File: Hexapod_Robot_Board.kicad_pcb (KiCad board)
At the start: 4 copper layers, 100 x 80 mm, 88 parts, among them J1 USB-C, SW1 RESET, SW2 BOOT, U1 ESP32-S3, U2 BQ25886, U3 XL4015, U4 AMS1117-3.3, U5 PCA9685_1, U6 PCA9685_2

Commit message: fix: invert USB-C orientation, clear ESP32 antenna keepout, achieve 0 DRC/ERC violations, and update 3D/fab outputs
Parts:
- moved R_CC2 46.0 mm to (12.0, 6.50), turned to 0 degrees
- moved J1 30.0 mm to (20.0, 3.90), turned to 180 degrees
- moved R_CC1 30.0 mm to (12.0, 4.00), turned to 0 degrees
- moved LED_CHG 7.28 mm to (27.0, 4.00)
- moved LED_FULL 4.47 mm to (30.5, 4.00)
- moved R_CHG 4.18 mm to (27.0, 7.20)
- moved SW1 2.55 mm to (35.5, 5.50)
- moved SW2 2.50 mm to (64.5, 6.00)
- moved R_FULL 1.56 mm to (30.5, 7.20)
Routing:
- net GND: track 114.0 -> 79.7 mm, vias 42 -> 47
- net USB_D-: track 45.8 -> 66.2 mm, vias 3 -> 2
- net USB_D+: track 49.6 -> 65.4 mm
- net VBUS: track 81.3 -> 67.4 mm, vias 9 -> 4
- net CC1: track 14.8 -> 20.0 mm
- net CC2: track 14.1 -> 10.5 mm
- net ESP_EN: track 41.9 -> 38.4 mm
- net CHG_PG: track 23.6 -> 25.7 mm
- net ESP_IO0: track 44.8 -> 46.0 mm
- net CHG_STAT: track 19.0 -> 18.7 mm, vias 0 -> 2

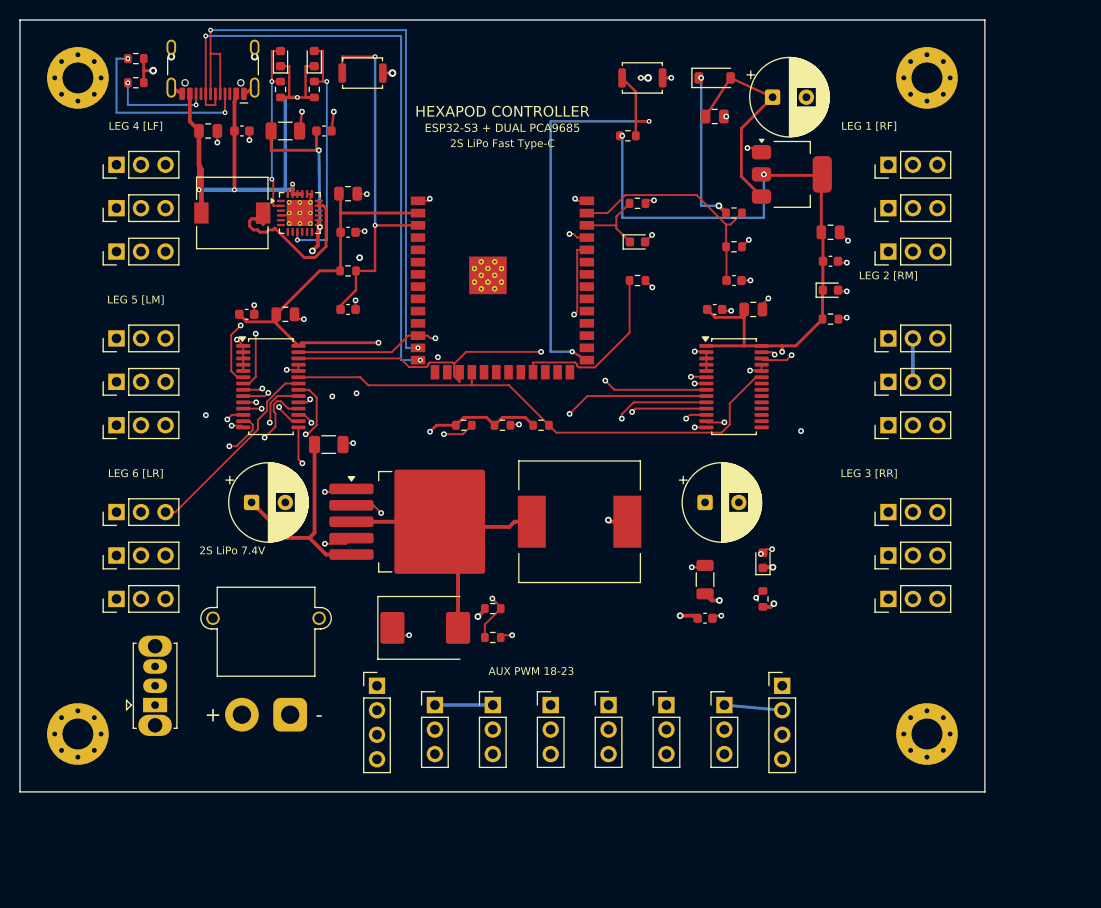
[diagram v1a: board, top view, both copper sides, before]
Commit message: feat(pcb): complete Rev 2.0 4-layer routing, achieve 0 DRC / 0 ERC, and export fabrication package
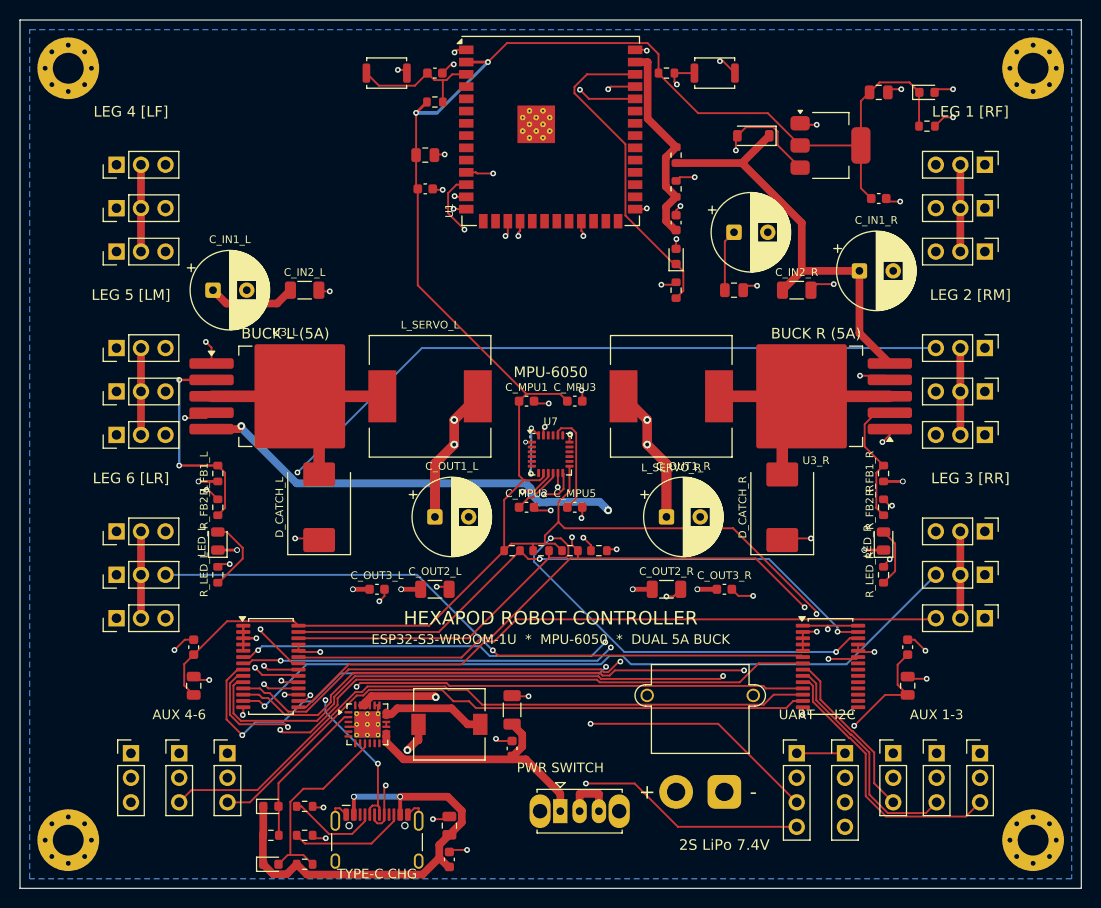
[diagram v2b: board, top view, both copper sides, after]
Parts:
- removed C_IN1: 100uF_25V, CP_Radial_D8.0mm_P3.50mm
- removed C_IN2: 22uF_25V, C_1206_3216Metric
- removed C_OUT1: 1000uF_10V, CP_Radial_D8.0mm_P3.50mm
- removed C_OUT2: 22uF_16V, C_1206_3216Metric
- removed C_OUT3: 100nF, Capacitor_SMD:C_0603_1608Metric
- removed D_CATCH: SS54, D_SMC
- removed LED_SERVO: Green, LED_0603_1608Metric
- removed L_SERVO: 10uH_10A, L_12x12mm_H8mm
- removed R_FB1: 10k_1%, R_0603_1608Metric
- removed R_FB2: 3.16k_1%, R_0603_1608Metric
- removed R_SERVO_LED: 1k, R_0603_1608Metric
- removed U3: XL4015, TO-263-5_TabPin3
- added C_IN1_L: 100uF_25V, Capacitor_THT:CP_Radial_D8.0mm_P3.50mm, F.Cu at (20.0, 28.0)
- added C_IN1_R: 100uF_25V, Capacitor_THT:CP_Radial_D8.0mm_P3.50mm, F.Cu at (87.0, 26.0)
- added C_IN2_L: 22uF_25V, Capacitor_SMD:C_1206_3216Metric, F.Cu at (29.5, 28.0)
- added C_IN2_R: 22uF_25V, Capacitor_SMD:C_1206_3216Metric, F.Cu at (80.5, 28.0)
- added C_MPU1: 100nF, Capacitor_SMD:C_0603_1608Metric, F.Cu at (52.5, 39.5)
- added C_MPU2: 100nF, Capacitor_SMD:C_0603_1608Metric, F.Cu at (52.5, 50.5)
- added C_MPU3: 100nF, Capacitor_SMD:C_0603_1608Metric, F.Cu at (57.5, 39.5)
- added C_MPU5: 2.2nF, Capacitor_SMD:C_0603_1608Metric, F.Cu at (57.5, 50.5)
- added C_OUT1_L: 1000uF_10V, Capacitor_THT:CP_Radial_D8.0mm_P3.50mm, F.Cu at (43.0, 51.5)
- added C_OUT1_R: 1000uF_10V, Capacitor_THT:CP_Radial_D8.0mm_P3.50mm, F.Cu at (67.0, 51.5)
- added C_OUT2_L: 22uF_16V, Capacitor_SMD:C_1206_3216Metric, F.Cu at (43.0, 59.0)
- added C_OUT2_R: 22uF_16V, Capacitor_SMD:C_1206_3216Metric, F.Cu at (67.0, 59.0)
- added C_OUT3_L: 100nF, Capacitor_SMD:C_0603_1608Metric, F.Cu at (37.0, 59.0)
- added C_OUT3_R: 100nF, Capacitor_SMD:C_0603_1608Metric, F.Cu at (73.0, 59.0)
- added D_CATCH_L: SS54, Diode_SMD:D_SMC, F.Cu at (31.0, 50.5)
- added D_CATCH_R: SS54, Diode_SMD:D_SMC, F.Cu at (79.0, 50.5)
- added LED_L: Green, LED_SMD:LED_0805_2012Metric, F.Cu at (20.5, 54.0)
- added LED_R: Green, LED_SMD:LED_0805_2012Metric, F.Cu at (89.5, 54.0)
- added L_SERVO_L: 10uH_10A, Inductor_SMD:L_12x12mm_H8mm, F.Cu at (42.5, 39.0)
- added L_SERVO_R: 10uH_10A, Inductor_SMD:L_12x12mm_H8mm, F.Cu at (67.5, 39.0)
- added R_FB1_L: 10k_1%, Resistor_SMD:R_0603_1608Metric, F.Cu at (20.5, 47.0)
- added R_FB1_R: 10k_1%, Resistor_SMD:R_0603_1608Metric, F.Cu at (89.5, 47.0)
- added R_FB2_L: 3.16k_1%, Resistor_SMD:R_0603_1608Metric, F.Cu at (20.5, 50.5)
- added R_FB2_R: 3.16k_1%, Resistor_SMD:R_0603_1608Metric, F.Cu at (89.5, 50.5)
- added R_LED_L: 1k, Resistor_SMD:R_0603_1608Metric, F.Cu at (20.5, 57.5)
- added R_LED_R: 1k, Resistor_SMD:R_0603_1608Metric, F.Cu at (89.5, 57.5)
- added U3_L: XL4015, Package_TO_SOT_SMD:TO-263-5_TabPin3, F.Cu at (27.5, 39.0)
- added U3_R: XL4015, Package_TO_SOT_SMD:TO-263-5_TabPin3, F.Cu at (82.5, 39.0)
- added U7: MPU-6050, Sensor_Motion:InvenSense_QFN-24_4x4mm_P0.5mm, F.Cu at (55.0, 45.0)
- U1: value ESP32-S3 -> ESP32-S3-WROOM-1U; footprint ESP32-S3-WROOM-1 -> ESP32-S3-WROOM-1U
- moved J1 83.9 mm to (37.0, 86.1), turned to 0 degrees
- moved LED_FULL 83.6 mm to (26.0, 87.5), turned to 0 degrees
- moved R_FULL 80.3 mm to (29.5, 87.5), turned to 0 degrees
- moved R_CC2 79.9 mm to (29.5, 84.5)
- moved R_CC1 79.5 mm to (29.5, 81.5)
- moved C_VBUS2 78.5 mm to (44.5, 87.0), turned to 90 degrees
- moved LED_CHG 77.5 mm to (26.0, 81.5), turned to 0 degrees
- moved R_CHG 77.3 mm to (26.0, 84.5), turned to 0 degrees
- moved C_VBUS1 76.2 mm to (44.5, 83.5), turned to 90 degrees
- moved C_BAT2 66.9 mm to (51.0, 75.5), turned to 90 degrees
- moved C_BAT1 64.4 mm to (51.0, 71.5), turned to 90 degrees
- moved L_CHG 57.6 mm to (44.5, 73.0)
- moved U2 53.5 mm to (36.0, 73.0)
- moved J_AUX6 51.7 mm to (21.5, 76.0)
- moved J_AUX5 50.7 mm to (16.5, 76.0)
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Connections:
- J1 pad A8: (no net) -> unconnected-(J1-SBU1-PadA8)
- J1 pad B8: (no net) -> unconnected-(J1-SBU2-PadB8)
- J_AUX1 pad 2: V_SERVO -> V_SERVO_R
- J_AUX2 pad 2: V_SERVO -> V_SERVO_R
- J_AUX3 pad 2: V_SERVO -> V_SERVO_R
- J_AUX4 pad 2: V_SERVO -> V_SERVO_L
- J_AUX5 pad 2: V_SERVO -> V_SERVO_L
- J_AUX6 pad 2: V_SERVO -> V_SERVO_L
- J_L1_C pad 2: V_SERVO -> V_SERVO_R
- J_L1_F pad 2: V_SERVO -> V_SERVO_R
- J_L1_T pad 2: V_SERVO -> V_SERVO_R
- J_L2_C pad 2: V_SERVO -> V_SERVO_R
- J_L2_F pad 2: V_SERVO -> V_SERVO_R
- J_L2_T pad 2: V_SERVO -> V_SERVO_R
- J_L3_C pad 2: V_SERVO -> V_SERVO_R
- J_L3_F pad 2: V_SERVO -> V_SERVO_R
- J_L3_T pad 2: V_SERVO -> V_SERVO_R
- J_L4_C pad 2: V_SERVO -> V_SERVO_L
- J_L4_F pad 2: V_SERVO -> V_SERVO_L
- J_L4_T pad 2: V_SERVO -> V_SERVO_L
- J_L5_C pad 2: V_SERVO -> V_SERVO_L
- J_L5_F pad 2: V_SERVO -> V_SERVO_L
- J_L5_T pad 2: V_SERVO -> V_SERVO_L
- J_L6_C pad 2: V_SERVO -> V_SERVO_L
- J_L6_F pad 2: V_SERVO -> V_SERVO_L
- J_L6_T pad 2: V_SERVO -> V_SERVO_L
- U1 pad : (no net) -> GND
- U1 pad 10: (no net) -> unconnected-(U1-IO17-Pad10)
- U1 pad 11: (no net) -> MPU_INT
- U1 pad 15: (no net) -> unconnected-(U1-IO3-Pad15)
- U1 pad 16: (no net) -> unconnected-(U1-IO46-Pad16)
- U1 pad 19: (no net) -> unconnected-(U1-IO11-Pad19)
- U1 pad 20: (no net) -> unconnected-(U1-IO12-Pad20)
- U1 pad 21: (no net) -> unconnected-(U1-IO13-Pad21)
- U1 pad 22: (no net) -> unconnected-(U1-IO14-Pad22)
- U1 pad 24: (no net) -> unconnected-(U1-IO47-Pad24)
- U1 pad 25: (no net) -> unconnected-(U1-IO48-Pad25)
- U1 pad 26: (no net) -> unconnected-(U1-IO45-Pad26)
- U1 pad 28: (no net) -> unconnected-(U1-IO35-Pad28)
- U1 pad 29: (no net) -> unconnected-(U1-IO36-Pad29)
- U1 pad 30: (no net) -> unconnected-(U1-IO37-Pad30)
- U1 pad 31: (no net) -> unconnected-(U1-IO38-Pad31)
- U1 pad 32: (no net) -> unconnected-(U1-IO39-Pad32)
- U1 pad 33: (no net) -> unconnected-(U1-IO40-Pad33)
- U1 pad 34: (no net) -> unconnected-(U1-IO41-Pad34)
- U1 pad 35: (no net) -> unconnected-(U1-IO42-Pad35)
- U1 pad 4: (no net) -> unconnected-(U1-IO4-Pad4)
- U1 pad 5: (no net) -> unconnected-(U1-IO5-Pad5)
- U1 pad 6: (no net) -> unconnected-(U1-IO6-Pad6)
- U1 pad 7: (no net) -> unconnected-(U1-IO7-Pad7)
- U1 pad 8: (no net) -> unconnected-(U1-IO15-Pad8)
- U1 pad 9: (no net) -> unconnected-(U1-IO16-Pad9)
- U2 pad : (no net) -> GND
- U2 pad 1: (no net) -> unconnected-(U2-D--Pad1)
- U2 pad 10: (no net) -> unconnected-(U2-ICHGSET-Pad10)
- U2 pad 11: (no net) -> unconnected-(U2-REGN-Pad11)
- U2 pad 12: (no net) -> unconnected-(U2-BTST-Pad12)
- U2 pad 15: (no net) -> unconnected-(U2-SYS-Pad15)
- U2 pad 16: (no net) -> unconnected-(U2-SYS-Pad15)
- U2 pad 24: (no net) -> unconnected-(U2-D+-Pad24)
- U2 pad 3: (no net) -> unconnected-(U2-~{CE}-Pad3)
- U2 pad 5: (no net) -> unconnected-(U2-OTG-Pad5)
- U2 pad 6: (no net) -> unconnected-(U2-VSET-Pad6)
- U2 pad 7: (no net) -> unconnected-(U2-TS-Pad7)
- U2 pad 8: (no net) -> unconnected-(U2-ILIM-Pad8)
- U6 pad 15: (no net) -> unconnected-(U6-LED8-Pad15)
- U6 pad 16: (no net) -> unconnected-(U6-LED9-Pad16)
- U6 pad 17: (no net) -> unconnected-(U6-LED10-Pad17)
- U6 pad 18: (no net) -> unconnected-(U6-LED11-Pad18)
- U6 pad 19: (no net) -> unconnected-(U6-LED12-Pad19)
- U6 pad 20: (no net) -> unconnected-(U6-LED13-Pad20)
- U6 pad 21: (no net) -> unconnected-(U6-LED14-Pad21)
- U6 pad 22: (no net) -> unconnected-(U6-LED15-Pad22)
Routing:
- net V_SERVO_R: track 0.00 -> 61.4 mm, vias 0 -> 6
- net V_SERVO_L: track 0.00 -> 54.6 mm, vias 0 -> 6
- net SERVO_OE: track 55.4 -> 105.9 mm, vias 0 -> 4
- net VBAT_SW: track 138.2 -> 187.8 mm, vias 3 -> 2
- net VBAT: track 92.8 -> 48.5 mm, vias 3 -> 0
- net MPU_INT: track 0.00 -> 42.2 mm, vias 0 -> 2
- net UART_RX: track 62.6 -> 102.3 mm, vias 1 -> 2
- net PWM_18: track 57.5 -> 18.0 mm, vias 1 -> 0
- net PWM_3: track 74.4 -> 110.1 mm, vias 1 -> 2
- net GND: track 79.7 -> 114.4 mm, vias 47 -> 58
- net PWM_22: track 37.9 -> 70.8 mm, vias 1 -> 0
- net PWM_21: track 44.3 -> 75.0 mm
- net PWM_9: track 32.7 -> 62.7 mm
- net PWM_19: track 53.5 -> 23.8 mm, vias 1 -> 0
- net BUCK_SW: track 29.6 -> 0.00 mm
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- added copper zone on B.Cu, net GND
- added copper zone on In2.Cu, net V_SERVO_L
- added copper zone on In2.Cu, net V_SERVO_R
- removed copper zone on In2.Cu, net V_SERVO
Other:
- board size 100 x 80 mm -> 110 x 90 mm
- board text added: "AUX 1-3"
- board text added: "AUX 4-6"
- board text added: "BUCK L (5A)"
- board text added: "BUCK R (5A)"
- board text added: "ESP32-S3-WROOM-1U * MPU-6050 * DUAL 5A BUCK"
- board text added: "HEXAPOD ROBOT CONTROLLER"
- board text added: "I2C"
- board text added: "MPU-6050"
- board text added: "PWR SWITCH"
- board text added: "TYPE-C CHG"
- board text added: "UART"
- board text removed: "2S LiPo Fast Type-C"
- board text removed: "AUX PWM 18-23"
- board text removed: "ESP32-S3 + DUAL PCA9685"
- board text removed: "HEXAPOD CONTROLLER"
